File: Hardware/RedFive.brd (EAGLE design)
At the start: 68.6 x 53.3 mm, 137 parts, among them IC3 LM1117, J1 FEMALE 2x3, J2 USB Female Type C Connector, J3 POWER_JACKSUPER_BOMB_DIGITY, J5 JTAG, Q1 1.1A/60V/600mΩ, U2 1.8V, U3 AP2112-3.3V, U4 FE310, U5 32MB, Y1 32.768KHZ, Y2 16MHz

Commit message: post design review changes
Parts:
- added JP1: JUMPER-SMT_2_NO_NO-SILK, SparkFun-Jumpers:SMT-JUMPER_2_NO_NO-SILK
- moved U$42 3.81 mm to (43.7, 42.2)
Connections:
- net USBVCC: now also JP1.2
- net VUSB: now also JP1.1
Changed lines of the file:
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@@
 <element name="U$40" library="buzzard_labels (6)" package="TXO28" value="" x="60.96" y="43.815" smashed="yes" rot="R90"/>
 <element name="U$41" library="buzzard_labels (6)" package="VIN6" value="" x="45.72" y="4.572" smashed="yes" rot="R90"/>
-<element name="U$42" library="buzzard_labels (6)" package="_#PWM30" value="" x="47.498" y="42.164" smashed="yes" rot="R90"/>
+<element name="U$42" library="buzzard_labels (6)" package="_#PWM30" value="" x="43.688" y="42.164" smashed="yes" rot="R90"/>
 <element name="U$43" library="buzzard_labels (6)" package="NC7" value="" x="23.876" y="44.958" smashed="yes" rot="R90"/>
 <element name="U$45" library="buzzard_labels (7)" package="133" value="" x="32.432" y="35.941" smashed="yes" rot="R90"/>
@@
 <attribute name="PROD_ID" value="CAP-11015" x="10.16" y="43.18" size="1.778" layer="27" rot="R180" display="off"/>
 </element>
+<element name="JP1" library="SparkFun-Jumpers" package="SMT-JUMPER_2_NO_NO-SILK" value="JUMPER-SMT_2_NO_NO-SILK" x="-22.86" y="-20.32"/>
 </elements>
 <signals>
@@
 <wire x1="8.128" y1="29.845" x2="9.522" y2="29.845" width="0.2032" layer="1"/>
 <wire x1="9.522" y1="29.845" x2="9.652" y2="29.715" width="0.2032" layer="1"/>
+<contactref element="JP1" pad="2"/>
+<wire x1="7.45" y1="26.924" x2="-22.4536" y2="-20.32" width="0" layer="19" extent="1-1"/>
 </signal>
 <signal name="VUSB">
@@
 <wire x1="7.62" y1="41.402" x2="7.493" y2="41.275" width="0.381" layer="16"/>
 <wire x1="7.493" y1="36.957" x2="7.493" y2="36.92" width="0.381" layer="1"/>
+<contactref element="JP1" pad="1"/>
+<wire x1="3.39" y1="29.845" x2="-23.2664" y2="-20.32" width="0" layer="19" extent="1-1"/>
 </signal>
 <signal name="N$1">

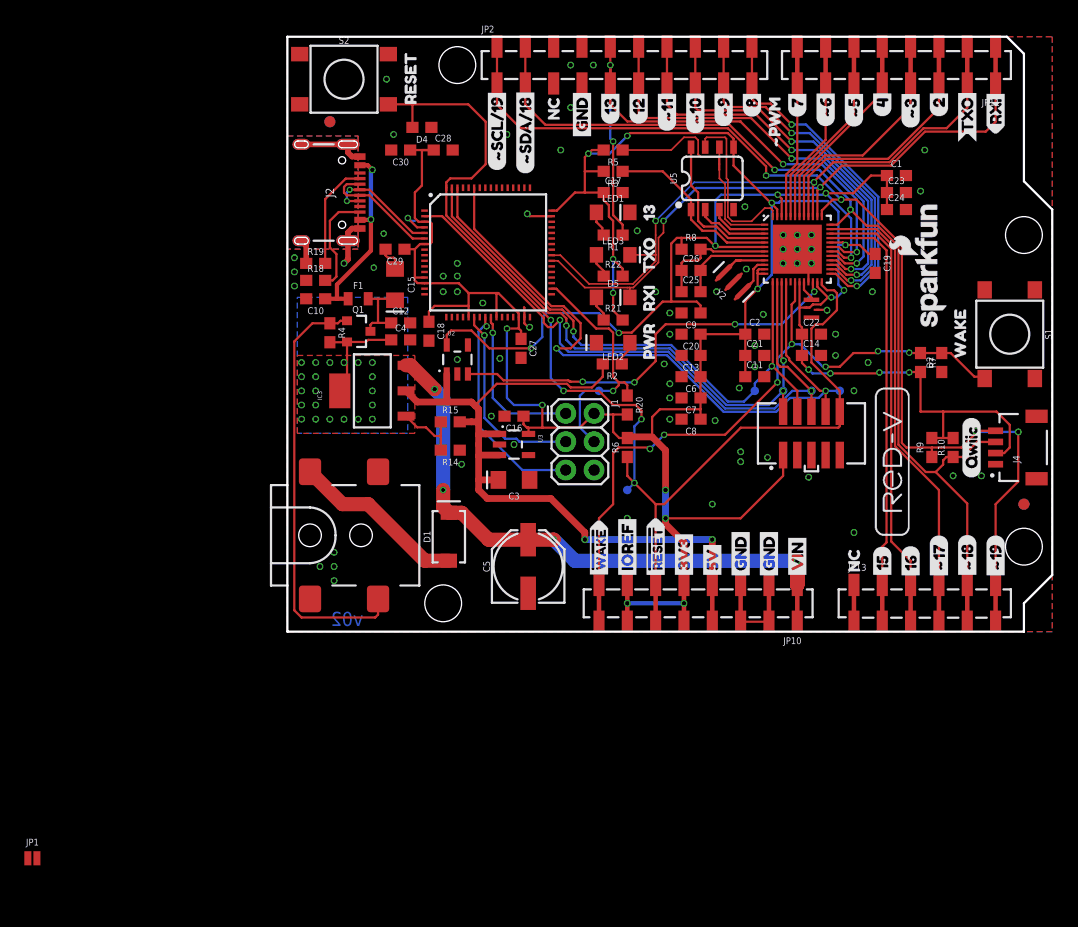
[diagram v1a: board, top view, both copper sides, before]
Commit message: post checklist changes, protos ordered
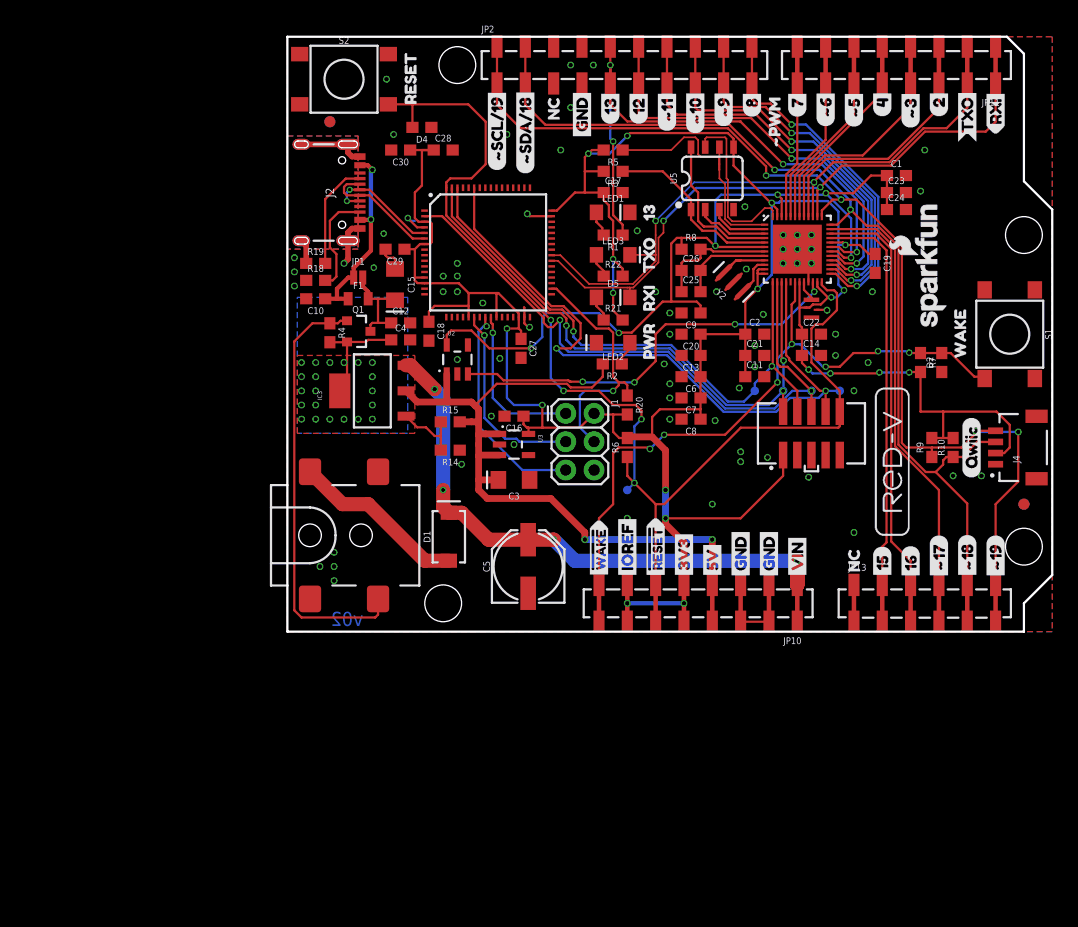
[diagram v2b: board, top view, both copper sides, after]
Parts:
- removed TP8: TEST-POINT3, SparkFun-Connectors:PAD.03X.03
- moved JP1 59.7 mm to (6.35, 31.8)
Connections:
- net DBG_RESET: no longer TP8.P$1
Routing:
- net USBVCC: track 7.14 -> 9.25 mm
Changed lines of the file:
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@@
 <layer number="27" name="tValues" color="7" fill="1" visible="yes" active="yes"/>
 <layer number="28" name="bValues" color="7" fill="1" visible="yes" active="yes"/>
-<layer number="29" name="tStop" color="2" fill="3" visible="no" active="yes"/>
-<layer number="30" name="bStop" color="5" fill="6" visible="no" active="yes"/>
-<layer number="31" name="tCream" color="7" fill="4" visible="no" active="yes"/>
-<layer number="32" name="bCream" color="7" fill="5" visible="no" active="yes"/>
+<layer number="29" name="tStop" color="2" fill="3" visible="yes" active="yes"/>
+<layer number="30" name="bStop" color="5" fill="6" visible="yes" active="yes"/>
+<layer number="31" name="tCream" color="7" fill="4" visible="yes" active="yes"/>
+<layer number="32" name="bCream" color="7" fill="5" visible="yes" active="yes"/>
 <layer number="33" name="tFinish" color="6" fill="3" visible="yes" active="yes"/>
 <layer number="34" name="bFinish" color="6" fill="6" visible="yes" active="yes"/>
@@
 <layer number="49" name="ReferenceLC" color="13" fill="1" visible="yes" active="yes"/>
 <layer number="50" name="ReferenceLS" color="12" fill="1" visible="yes" active="yes"/>
-<layer number="51" name="tDocu" color="6" fill="1" visible="no" active="yes"/>
+<layer number="51" name="tDocu" color="6" fill="1" visible="yes" active="yes"/>
 <layer number="52" name="bDocu" color="7" fill="1" visible="yes" active="yes"/>
 <layer number="91" name="Nets" color="2" fill="1" visible="no" active="no"/>
@@
 <layer number="115" name="ReferenceISLANDS" color="7" fill="1" visible="no" active="no"/>
 <layer number="116" name="Patch_BOT" color="7" fill="1" visible="no" active="no"/>
-<layer number="117" name="PM_Ref" color="26" fill="1" visible="yes" active="yes"/>
+<layer number="117" name="PM_Ref" color="26" fill="1" visible="no" active="yes"/>
 <layer number="118" name="Rect_Pads" color="7" fill="1" visible="no" active="no"/>
-<layer number="119" name="PF_Ref" color="31" fill="1" visible="yes" active="yes"/>
-<layer number="120" name="WFL_Ref" color="25" fill="1" visible="yes" active="yes"/>
+<layer number="119" name="PF_Ref" color="31" fill="1" visible="no" active="yes"/>
+<layer number="120" name="WFL_Ref" color="25" fill="1" visible="no" active="yes"/>
 <layer number="121" name="_tsilk" color="7" fill="1" visible="no" active="no"/>
 <layer number="122" name="_bsilk" color="7" fill="1" visible="no" active="no"/>
@@
 <attribute name="VALUE" value="FEMALE 2x3" x="24.96" y="19.57" size="1.778" layer="27" rot="R270" display="off"/>
 </element>
-<element name="TP8" library="SparkFun-Connectors" package="PAD.03X.03" value="TEST-POINT3" x="27.94" y="21.59" rot="MR0"/>
 <element name="R20" library="SparkFun-Resistors" package="0603" value="100k" x="30.48" y="20.32" rot="R270">
 <attribute name="PROD_ID" value="RES-07828" x="30.48" y="20.32" size="1.778" layer="27" rot="R270" display="off"/>
@@
 <attribute name="PROD_ID" value="CAP-11015" x="10.16" y="43.18" size="1.778" layer="27" rot="R180" display="off"/>
 </element>
-<element name="JP1" library="SparkFun-Jumpers" package="SMT-JUMPER_2_NO_NO-SILK" value="JUMPER-SMT_2_NO_NO-SILK" x="-22.86" y="-20.32"/>
+<element name="JP1" library="SparkFun-Jumpers" package="SMT-JUMPER_2_NO_NO-SILK" value="JUMPER-SMT_2_NO_NO-SILK" x="6.35" y="31.75"/>
 </elements>
 <signals>
@@
 <wire x1="35.56" y1="4.19" x2="35.56" y2="8" width="0.6096" layer="1"/>
 <wire x1="32.705" y1="17.46" x2="33.909" y2="16.256" width="0.6096" layer="1"/>
-<wire x1="33.909" y1="16.256" x2="33.909" y2="12.7" width="0.6096" layer="1"/>
 <wire x1="35.56" y1="0.89" x2="35.56" y2="2.54" width="0.2032" layer="1"/>
 <wire x1="30.48" y1="2.54" x2="30.48" y2="0.89" width="0.2032" layer="1"/>
@@
 <wire x1="12.7" y1="43.18" x2="12.065" y2="43.18" width="0.2032" layer="1"/>
 <wire x1="12.7" y1="43.18" x2="11.01" y2="43.18" width="0.2032" layer="1"/>
+<wire x1="33.909" y1="16.256" x2="33.909" y2="12.7" width="0.6096" layer="1"/>
 </signal>
 <signal name="VIN">
@@
 <wire x1="9.522" y1="29.845" x2="9.652" y2="29.715" width="0.2032" layer="1"/>
 <contactref element="JP1" pad="2"/>
-<wire x1="7.45" y1="26.924" x2="-22.4536" y2="-20.32" width="0" layer="19" extent="1-1"/>
+<wire x1="6.7564" y1="31.75" x2="6.7564" y2="30.9626" width="0.381" layer="1"/>
+<wire x1="7.25" y1="30.469" x2="7.25" y2="29.845" width="0.381" layer="1"/>
+<wire x1="6.7564" y1="30.9626" x2="7.25" y2="30.469" width="0.381" layer="1"/>
 </signal>
 <signal name="VUSB">
@@
 <wire x1="7.202" y1="41.82" x2="6.504" y2="41.82" width="0.381" layer="1"/>
 <wire x1="7.493" y1="36.92" x2="7.493" y2="34.163" width="0.381" layer="1"/>
-<wire x1="4.445" y1="31.115" x2="4.445" y2="29.845" width="0.381" layer="1"/>
-<wire x1="7.493" y1="34.163" x2="4.445" y2="31.115" width="0.381" layer="1"/>
 <wire x1="7.62" y1="41.402" x2="7.493" y2="41.275" width="0.381" layer="16"/>
 <wire x1="7.493" y1="36.957" x2="7.493" y2="36.92" width="0.381" layer="1"/>
 <contactref element="JP1" pad="1"/>
-<wire x1="3.39" y1="29.845" x2="-23.2664" y2="-20.32" width="0" layer="19" extent="1-1"/>
+<wire x1="4.445" y1="30.734" x2="5.461" y2="31.75" width="0.381" layer="1"/>
+<wire x1="5.461" y1="31.75" x2="5.9436" y2="31.75" width="0.381" layer="1"/>
+<wire x1="4.445" y1="29.845" x2="4.445" y2="30.734" width="0.381" layer="1"/>
+<wire x1="5.9436" y1="32.6136" x2="5.9436" y2="31.75" width="0.381" layer="1"/>
+<wire x1="7.493" y1="34.163" x2="5.9436" y2="32.6136" width="0.381" layer="1"/>
 </signal>
 <signal name="N$1">
@@
 <contactref element="U$44" pad="34"/>
 <contactref element="R20" pad="1"/>
-<contactref element="TP8" pad="P$1"/>
 <wire x1="24.114" y1="30.75" x2="27.686" y2="27.178" width="0.2032" layer="1"/>
 <wire x1="27.686" y1="27.178" x2="28.829" y2="27.178" width="0.2032" layer="1"/>
@@
 <wire x1="27.5" y1="17.03" x2="26.2255" y2="18.3045" width="0.2032" layer="16"/>
 <wire x1="26.2255" y1="21.1455" x2="26.67" y2="21.59" width="0.2032" layer="16"/>
-<wire x1="26.67" y1="21.59" x2="27.94" y2="21.59" width="0.2032" layer="16"/>
 <wire x1="26.2255" y1="18.3045" x2="26.2255" y2="21.1455" width="0.2032" layer="16"/>
 <wire x1="29.21" y1="22.86" x2="29.718" y2="22.352" width="0.2032" layer="1"/>
@@
 <wire x1="30.48" y1="22.098" x2="30.48" y2="21.17" width="0.2032" layer="1"/>
 <wire x1="29.718" y1="22.352" x2="30.226" y2="22.352" width="0.2032" layer="1"/>
-<wire x1="27.94" y1="21.59" x2="29.21" y2="21.59" width="0.2032" layer="16"/>
 <via x="29.21" y="21.59" extent="1-16" drill="0.35"/>
 <wire x1="29.21" y1="21.59" x2="29.718" y2="22.098" width="0.2032" layer="1"/>
 <wire x1="29.718" y1="22.098" x2="29.718" y2="22.352" width="0.2032" layer="1"/>
+<wire x1="26.67" y1="21.59" x2="26.67" y2="21.59" width="0.2032" layer="16"/>
+<wire x1="26.67" y1="21.59" x2="29.21" y2="21.59" width="0.2032" layer="16"/>
 </signal>
 <signal name="DBG_SWDIO">

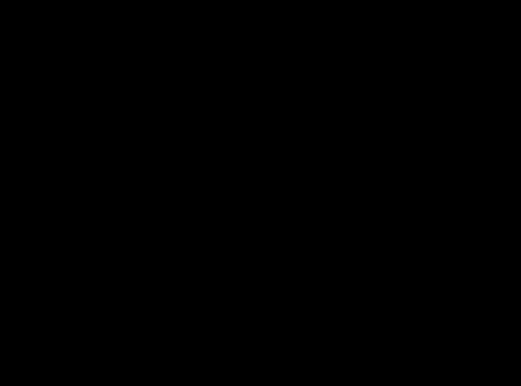
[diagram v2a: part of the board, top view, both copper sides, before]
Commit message: adding 5V test point
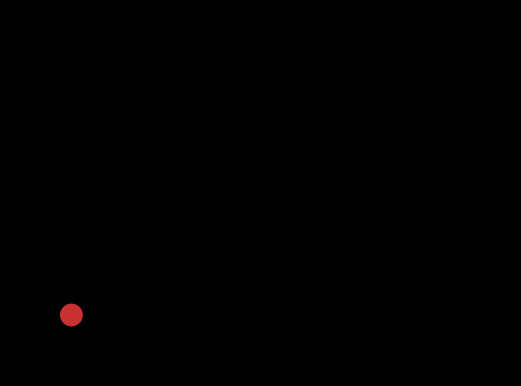
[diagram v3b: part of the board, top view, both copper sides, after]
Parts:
- added TP8: TEST-POINT3, SparkFun-Connectors:PAD.03X.03
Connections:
- net 5V: now also TP8.P$1
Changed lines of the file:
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@@
 </element>
 <element name="JP1" library="SparkFun-Jumpers" package="SMT-JUMPER_2_NO_NO-SILK" value="JUMPER-SMT_2_NO_NO-SILK" x="6.35" y="31.75"/>
+<element name="TP8" library="SparkFun-Connectors" package="PAD.03X.03" value="TEST-POINT3" x="-19.05" y="-24.13"/>
 </elements>
 <signals>
@@
 <wire x1="25.0698" y1="22.225" x2="18.78" y2="22.225" width="0.2032" layer="1"/>
 <wire x1="28.28" y1="22.86" x2="27.3148" y2="21.8948" width="0.2032" layer="1"/>
+<contactref element="TP8" pad="P$1"/>
+<wire x1="1.27" y1="19.05" x2="-19.05" y2="-24.13" width="0" layer="19" extent="1-1"/>
+<wire x1="2.54" y1="19.05" x2="1.27" y2="19.05" width="0" layer="19" extent="1-1"/>
+<wire x1="2.54" y1="20.32" x2="2.54" y2="19.05" width="0" layer="19" extent="1-1"/>
+<wire x1="2.54" y1="21.59" x2="2.54" y2="20.32" width="0" layer="19" extent="1-1"/>
+<wire x1="2.54" y1="22.86" x2="2.54" y2="21.59" width="0" layer="19" extent="1-1"/>
+<wire x1="2.54" y1="24.13" x2="2.54" y2="22.86" width="0" layer="19" extent="1-1"/>
+<wire x1="3.81" y1="24.13" x2="2.54" y2="24.13" width="0" layer="19" extent="1-1"/>
+<wire x1="5.08" y1="24.13" x2="3.81" y2="24.13" width="0" layer="19" extent="1-1"/>
+<wire x1="6.35" y1="24.13" x2="5.08" y2="24.13" width="0" layer="19" extent="1-1"/>
+<wire x1="7.62" y1="24.13" x2="6.35" y2="24.13" width="0" layer="19" extent="1-1"/>
+<wire x1="7.62" y1="22.86" x2="7.62" y2="24.13" width="0" layer="19" extent="1-1"/>
+<wire x1="7.62" y1="21.59" x2="7.62" y2="22.86" width="0" layer="19" extent="1-1"/>
+<wire x1="7.62" y1="20.32" x2="7.62" y2="21.59" width="0" layer="19" extent="1-1"/>
+<wire x1="7.62" y1="19.05" x2="7.62" y2="20.32" width="0" layer="19" extent="1-1"/>
+<wire x1="6.35" y1="19.05" x2="7.62" y2="19.05" width="0" layer="19" extent="1-1"/>
+<wire x1="5.08" y1="19.05" x2="6.35" y2="19.05" width="0" layer="19" extent="1-1"/>
+<wire x1="1.27" y1="24.13" x2="2.54" y2="24.13" width="0" layer="19" extent="1-1"/>
+<wire x1="1.27" y1="22.86" x2="2.54" y2="22.86" width="0" layer="19" extent="1-1"/>
+<wire x1="3.81" y1="19.05" x2="2.54" y2="19.05" width="0" layer="19" extent="1-1"/>
+<wire x1="1.27" y1="21.59" x2="2.54" y2="21.59" width="0" layer="19" extent="1-1"/>
+<wire x1="1.27" y1="20.32" x2="1.27" y2="19.05" width="0" layer="19" extent="1-1"/>
+<wire x1="3.81" y1="25.947" x2="3.81" y2="24.13" width="0" layer="19" extent="1-1"/>
+<wire x1="10.64" y1="21.59" x2="7.62" y2="21.59" width="0" layer="19" extent="1-1"/>
 </signal>
 <signal name="GND">

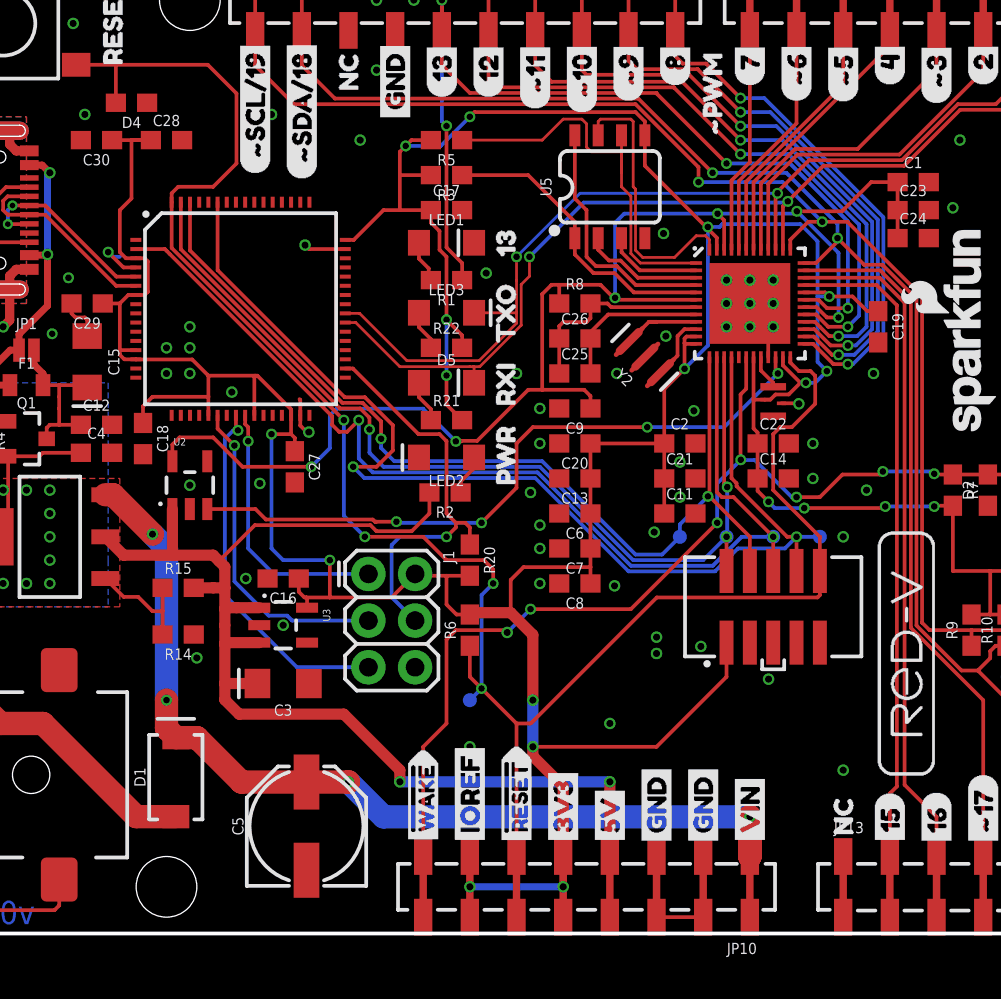
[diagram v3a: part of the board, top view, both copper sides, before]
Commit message: needs routing, post prototype changes
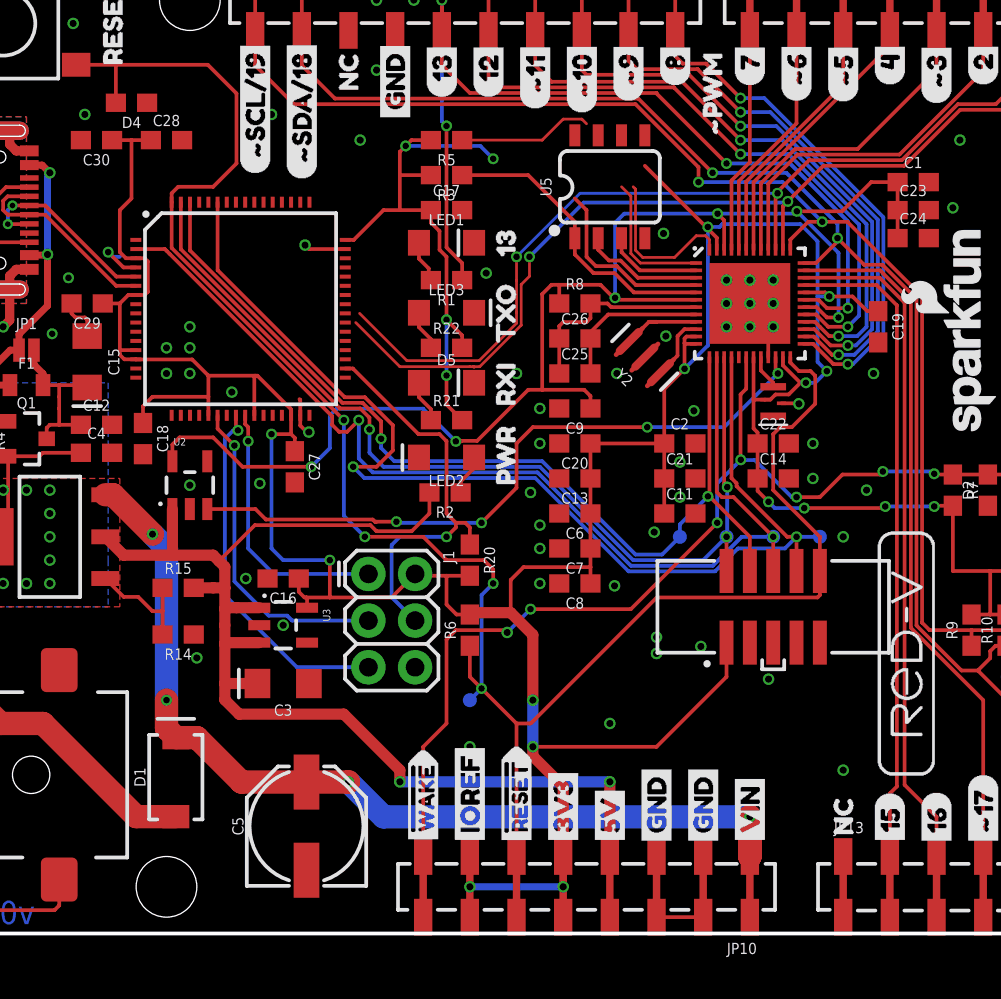
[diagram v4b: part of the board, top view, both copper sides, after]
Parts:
- J4: value (none) -> QWIIC_RIGHT_ANGLE
- U5: value 32MB -> 32MBit
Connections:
- net 3.3V: now also U5.8; no longer U5.5
- net QSPI_0: now also U5.5; no longer U5.8
- net QSPI_3: now also U5.7; no longer U5.6
- net QSPI_SCK: now also U5.6; no longer U5.7
- net RXI: now also LED3.C, U$44.40; no longer D5.C, U$44.39
- net TXO: now also D5.C, U$44.39; no longer LED3.C, U$44.40
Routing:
- net 3.3V: track 261.6 -> 248.3 mm
- net QSPI_3: track 22.2 -> 15.0 mm
- net QSPI_SCK: track 15.1 -> 8.81 mm
- net QSPI_0: track 13.5 -> 10.0 mm
- net TXO: track 58.0 -> 55.0 mm
- net RXI: track 59.3 -> 57.9 mm

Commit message: Pre design review-reds
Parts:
- removed TP1, TP2, TP3, TP4, TP5, TP6, TP7: TEST-POINT3, SparkFun-Connectors:PAD.03X.03
- J1: device SparkFun-Connectors:2X3 -> SparkFun-Connectors:2X3_POGO
- J5: value JTAG -> CORTEX_JTAG_DEBUG_PTH_NS; device SparkFun-Connectors:2X5-SMD-1.27MM -> SparkFun-Connectors:2X5-PTH-1.27MM-NO_SILK
- moved TP8 57.1 mm to (15.2, 21.6), flipped to the bottom
- moved U$47 3.81 mm to (32.4, 31.6)
- moved U$48 3.81 mm to (32.4, 27.4)
- moved J5 2.16 mm to (47.0, 15.6), turned to 0 degrees
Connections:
- net !RESET: no longer TP5.P$1
- net 3.3V: now also J1.P$2; no longer J1.2, TP6.P$1
- net DBG_RESET: now also J1.P$4; no longer J1.4
- net DBG_SWDCLK: now also J1.P$3; no longer J1.3
- net DBG_SWDIO: now also J1.P$1; no longer J1.1
- net DBG_SWO: now also J1.P$5; no longer J1.5
- net GND: now also J1.P$6; no longer J1.6, TP7.P$1
- net TCK: no longer TP2.P$1
- net TDI: no longer TP4.P$1
- net TDO: no longer TP3.P$1
- net TMS: no longer TP1.P$1
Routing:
- net 3.3V: track 248.3 -> 260.7 mm, vias 19 -> 20
- net QSPI_0: track 10.0 -> 16.4 mm, vias 0 -> 2
- net !RESET: track 109.3 -> 115.5 mm
- net QSPI_3: track 15.0 -> 19.6 mm
- net RXI: track 57.9 -> 61.7 mm
- net TMS: track 52.6 -> 56.1 mm
- net TDO: track 57.8 -> 61.2 mm
- net TCK: track 52.9 -> 56.1 mm
- net QSPI_SCK: track 8.81 -> 11.9 mm
- net TDI: track 62.6 -> 64.7 mm
- net TXO: track 55.0 -> 56.9 mm
- net 5V: track 78.9 -> 79.9 mm, vias 23 -> 24
